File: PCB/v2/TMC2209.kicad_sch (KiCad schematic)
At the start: 10 parts

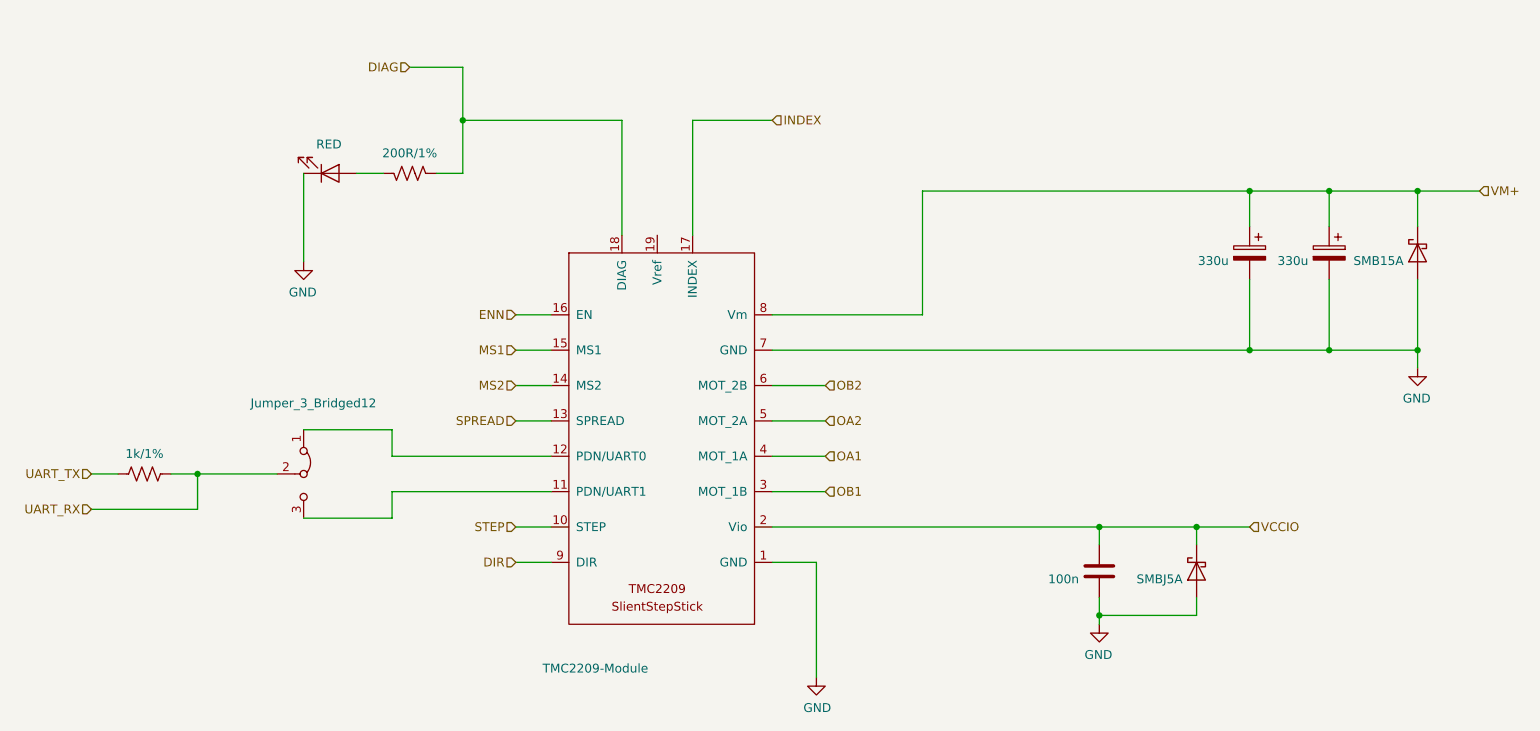
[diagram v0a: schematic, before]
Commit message: WIP updated symbols for tmc5106
Updated footprint for tmc5106,
need to check how motor wiring is done, might be wired up stupid before and that's gonna be sad
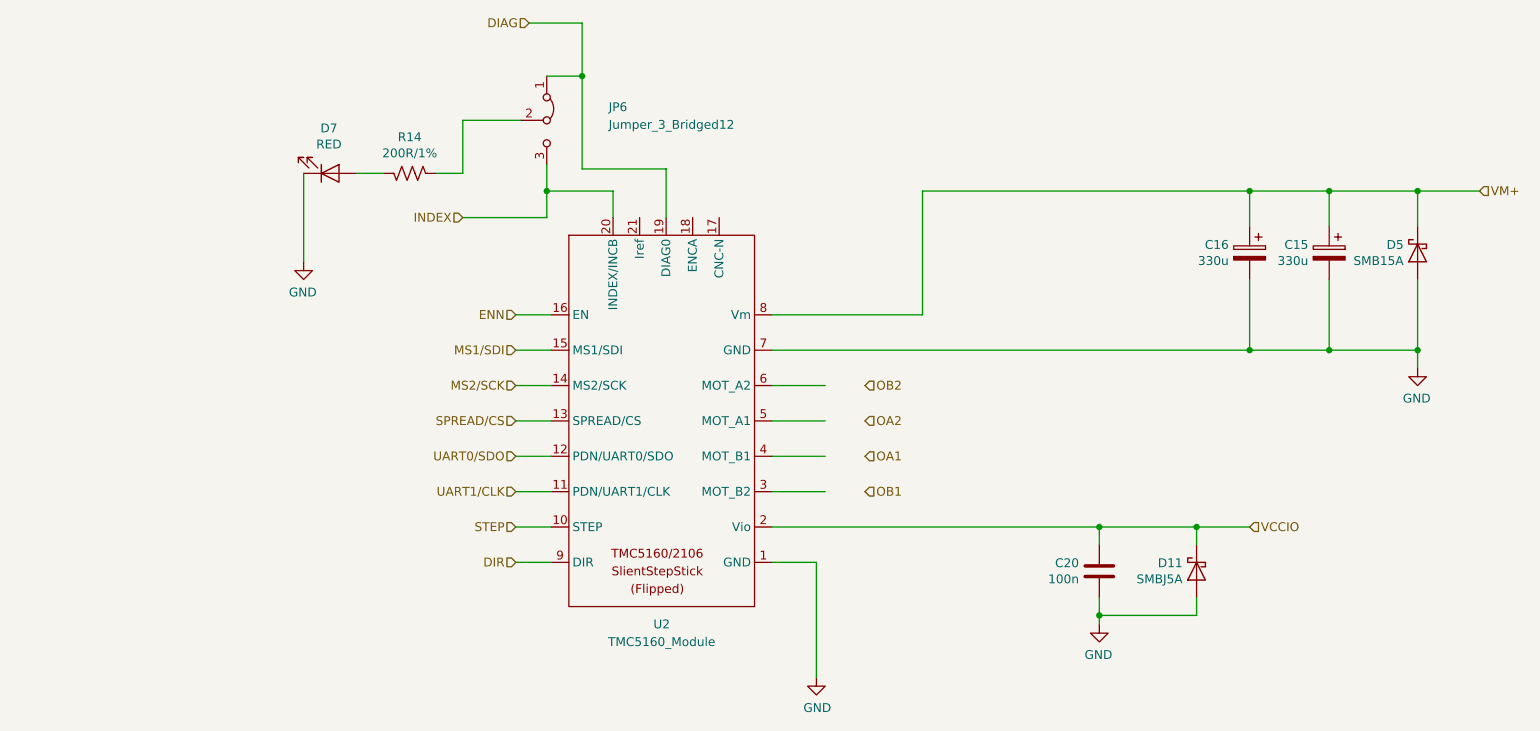
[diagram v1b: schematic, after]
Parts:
- removed ?: 1k/1%, Resistor_SMD:R_0603_1608Metric, symbol MMTK-rescue:R_US-Device-MMTK-rescue-MMTK-rescue
- removed ?: TMC2209-Module, MMTK:TMCC2209_Module, symbol MMTK:TMC2209-Module
- removed ?: Jumper_3_Bridged12, Jumper:SolderJumper-3_P1.3mm_Bridged12_Pad1.0x1.5mm_NumberLabels, symbol Jumper:Jumper_3_Bridged12
- added JP6: Jumper_3_Bridged12, Jumper:SolderJumper-3_P1.3mm_Bridged12_Pad1.0x1.5mm_NumberLabels, symbol Jumper:Jumper_3_Bridged12
- added U2: TMC5160_Module, MMTK:TMCC2209_Module_copy, symbol MMTK:TMC5160_Module
- gave numbers to parts that had none: 7
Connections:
- net DIAG: now also JP6.1 (A), U2.19 (DIAG0); no longer R14.2
- net DIR: now also U2.9 (DIR)
- net ENN: now also U2.16 (EN)
- net GND: now also U2.1 (GND), U2.7 (GND)
- net INDEX: now also JP6.3 (B), U2.20 (INDEX/INCB)
- net STEP: now also U2.10 (STEP)
- net VCCIO: now also U2.2 (Vio)
- net VM+: now also U2.8 (Vm)
- new net: JP6.2 (C), R14.2
- new net MS1/SDI: U2.15 (MS1/SDI)
- new net MS2/SCK: U2.14 (MS2/SCK)
- new net SPREAD/CS: U2.13 (SPREAD/CS)
- new net UART0/SDO: U2.12 (PDN/UART0/SDO)
- new net UART1/CLK: U2.11 (PDN/UART1/CLK)

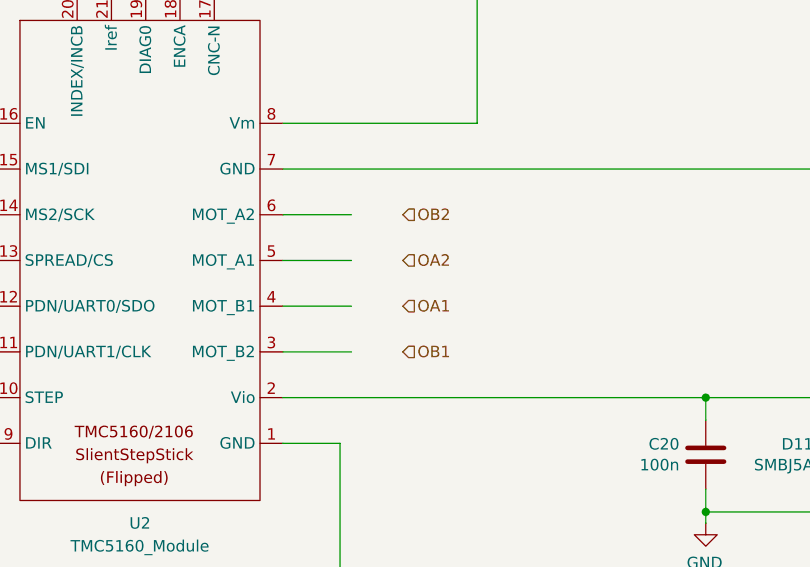
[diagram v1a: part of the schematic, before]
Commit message: Figured Out Motor Wiring
Updated motor wiring, naming on slient step stick is the same as tmc chips itself.
Phrases are A and B and 1/2 are the wires from the same phrase.
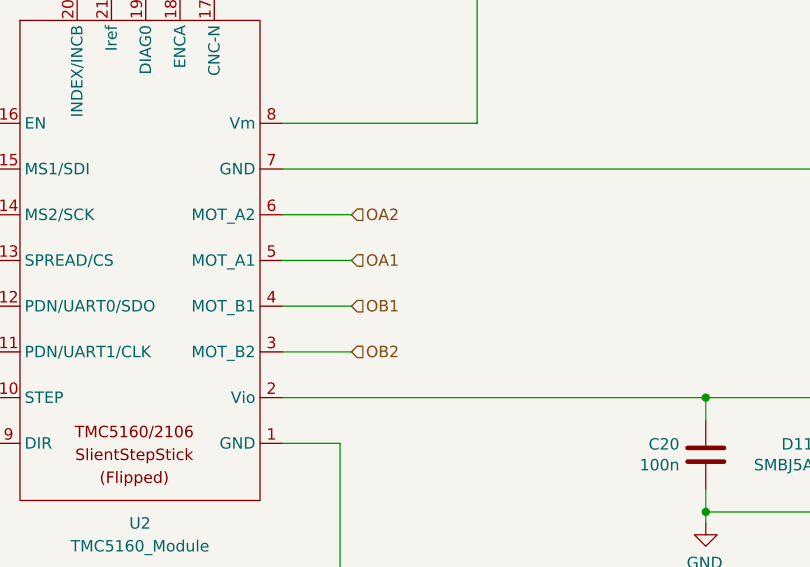
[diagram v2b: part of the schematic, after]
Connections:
- net OA1: now also U2.5 (MOT_A1)
- net OA2: now also U2.6 (MOT_A2)
- net OB1: now also U2.4 (MOT_B1)
- net OB2: now also U2.3 (MOT_B2)
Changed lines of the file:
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@@
     (effects (font (size 1.27 1.27)) (justify right))
   )
-  (hierarchical_label "OB1" (shape input) (at 165.735 109.22 0)
+  (hierarchical_label "OB1" (shape input) (at 160.02 104.14 0)
     (effects (font (size 1.27 1.27)) (justify left))
   )
@@
     (effects (font (size 1.27 1.27)) (justify left))
   )
-  (hierarchical_label "OA1" (shape input) (at 165.735 104.14 0)
+  (hierarchical_label "OA1" (shape input) (at 160.02 99.06 0)
     (effects (font (size 1.27 1.27)) (justify left))
   )
-  (hierarchical_label "OA2" (shape input) (at 165.735 99.06 0)
+  (hierarchical_label "OA2" (shape input) (at 160.02 93.98 0)
     (effects (font (size 1.27 1.27)) (justify left))
   )
@@
     (effects (font (size 1.27 1.27)) (justify right))
   )
-  (hierarchical_label "OB2" (shape input) (at 165.735 93.98 0)
+  (hierarchical_label "OB2" (shape input) (at 160.02 109.22 0)
     (effects (font (size 1.27 1.27)) (justify left))
   )
